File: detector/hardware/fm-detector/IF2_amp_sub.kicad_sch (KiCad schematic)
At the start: 7 parts, among them Q2 MMBT3904

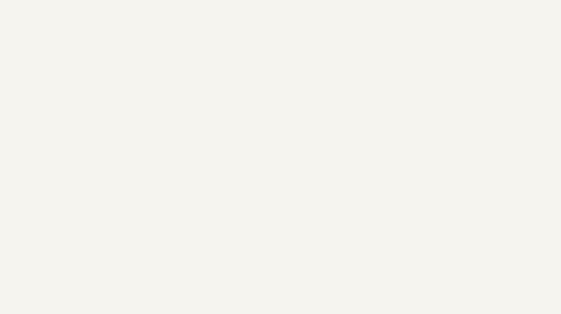
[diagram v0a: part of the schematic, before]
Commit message: Schematic for PCB-0010-0100
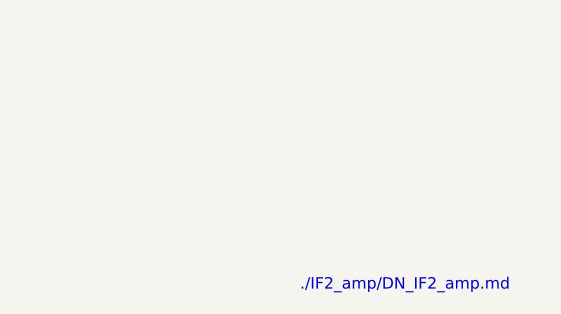
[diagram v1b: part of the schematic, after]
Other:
- note added: "./IF2_amp/DN_IF2_amp.md"
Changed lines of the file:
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@@
 		(title "IF2 Amplifier stage")
+	)
+	(text "./IF2_amp/DN_IF2_amp.md"
+		(exclude_from_sim no)
+		(at 115.57 129.54 0)
+		(effects
+			(font
+				(size 1.27 1.27)
+			)
+			(href "https://github.com/LieBtrau/MegawattKS_Radio_Design_101/blob/main/IF2_amp/DN_IF2_amp.md")
+		)
 	)
 	(junction
